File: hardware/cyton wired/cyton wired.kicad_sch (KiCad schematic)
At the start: 13 parts, among them J1 Conn_02x13_Odd_Even, J2 Conn_01x08, J3 Conn_01x04, J4 Conn_01x02, J5 Conn_01x04

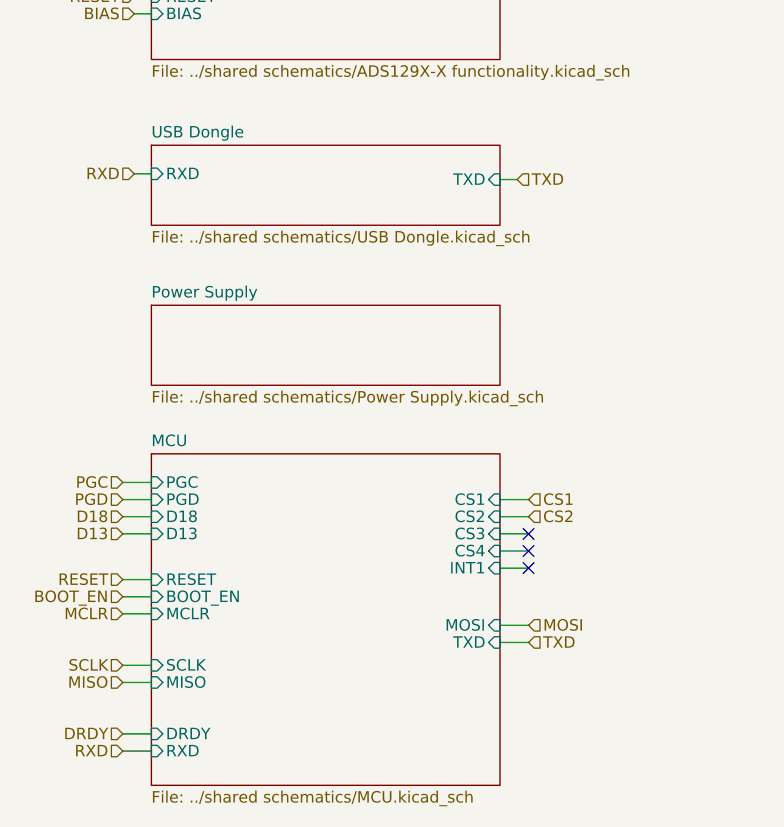
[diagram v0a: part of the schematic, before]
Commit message: fixed RX and TX pins configuration
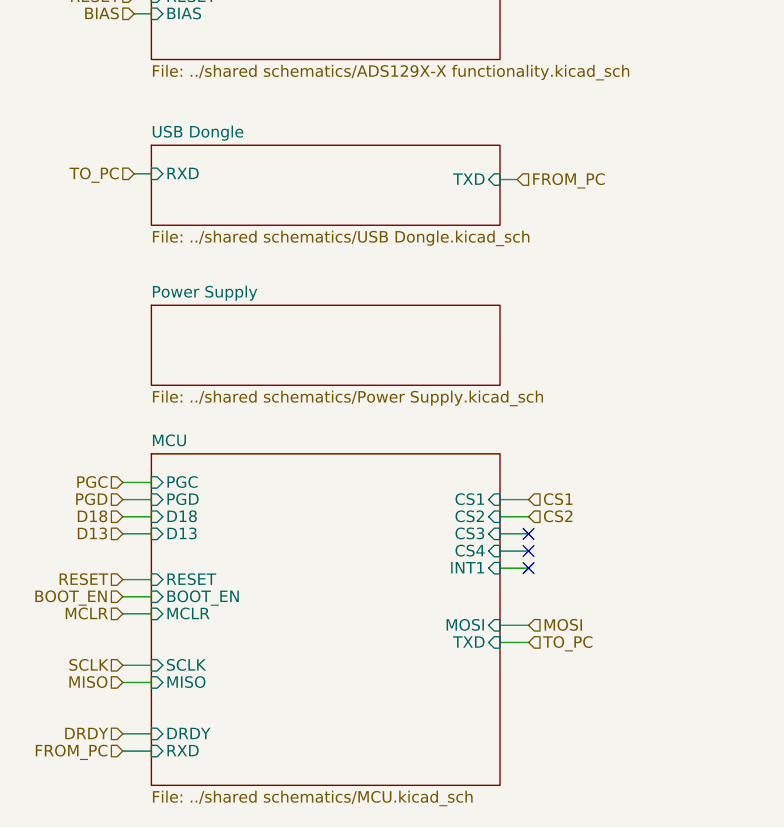
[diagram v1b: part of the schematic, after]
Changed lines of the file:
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@@
     (effects (font (size 1.27 1.27)) (justify left))
   )
-  (hierarchical_label "RXD" (shape input) (at 28.575 104.14 180) (fields_autoplaced)
+  (hierarchical_label "TO_PC" (shape input) (at 28.575 104.14 180) (fields_autoplaced)
     (effects (font (size 1.27 1.27)) (justify right))
   )
@@
     (effects (font (size 1.27 1.27)) (justify right))
   )
-  (hierarchical_label "TXD" (shape input) (at 71.12 104.775 0) (fields_autoplaced)
+  (hierarchical_label "FROM_PC" (shape input) (at 71.12 104.775 0) (fields_autoplaced)
     (effects (font (size 1.27 1.27)) (justify left))
   )
@@
     (effects (font (size 1.27 1.27)) (justify right))
   )
-  (hierarchical_label "RXD" (shape input) (at 27.305 168.275 180) (fields_autoplaced)
-    (effects (font (size 1.27 1.27)) (justify right))
-  )
-  (hierarchical_label "TXD" (shape input) (at 72.39 156.21 0) (fields_autoplaced)
-    (effects (font (size 1.27 1.27)) (justify left))
-  )
+  (hierarchical_label "FROM_PC" (shape input) (at 27.305 168.275 180) (fields_autoplaced)
+    (effects (font (size 1.27 1.27)) (justify right))
+  )
+  (hierarchical_label "TO_PC" (shape input) (at 72.39 156.21 0) (fields_autoplaced)
+    (effects (font (size 1.27 1.27)) (justify left))
+  )
